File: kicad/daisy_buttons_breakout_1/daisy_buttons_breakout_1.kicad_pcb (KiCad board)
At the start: 2 copper layers, 25 parts, among them J1 Conn_01x07_Pin, SW1 SW_Push, SW10 SW_Push, SW11 SW_Push, SW12 SW_Push, SW13 SW_Push, SW14 SW_Push, SW15 SW_Push, SW16 SW_Push, SW17 SW_Push, SW18 SW_Push, SW19 SW_Push, SW2 SW_Push, SW20 SW_Push, SW3 SW_Push, SW4 SW_Push, SW5 SW_Push, SW6 SW_Push, SW7 SW_Push, SW8 SW_Push, SW9 SW_Push, U1 MCP23017x-x-SO

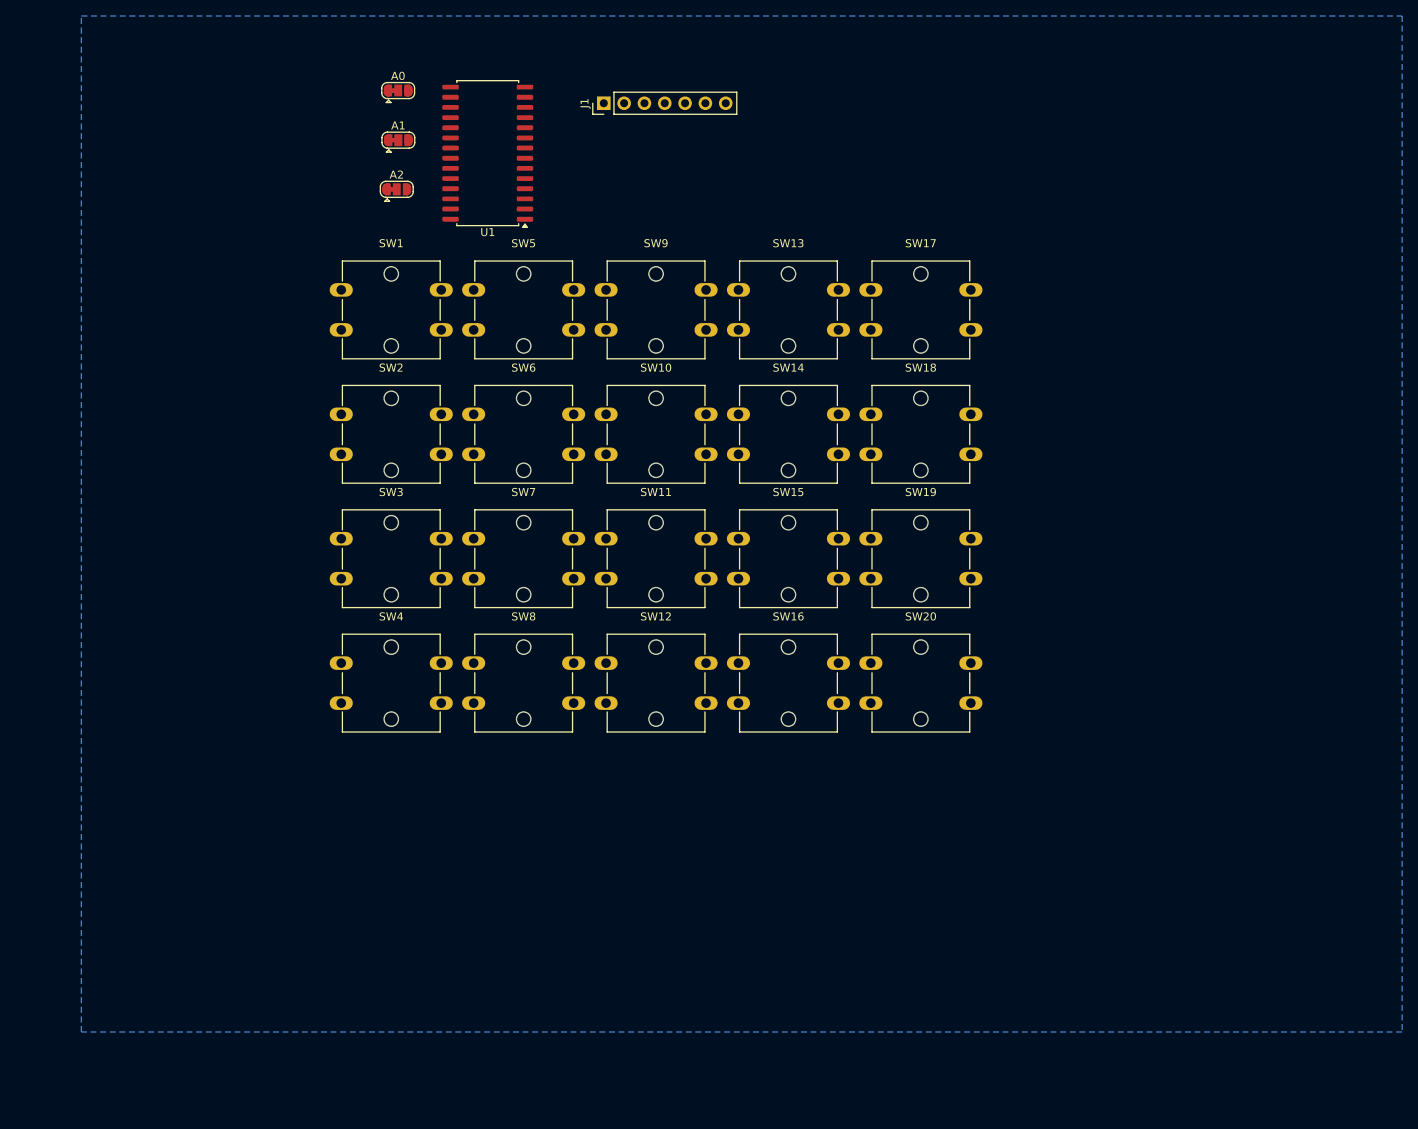
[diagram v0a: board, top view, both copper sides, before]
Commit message: Finish carrier PCB for daisy
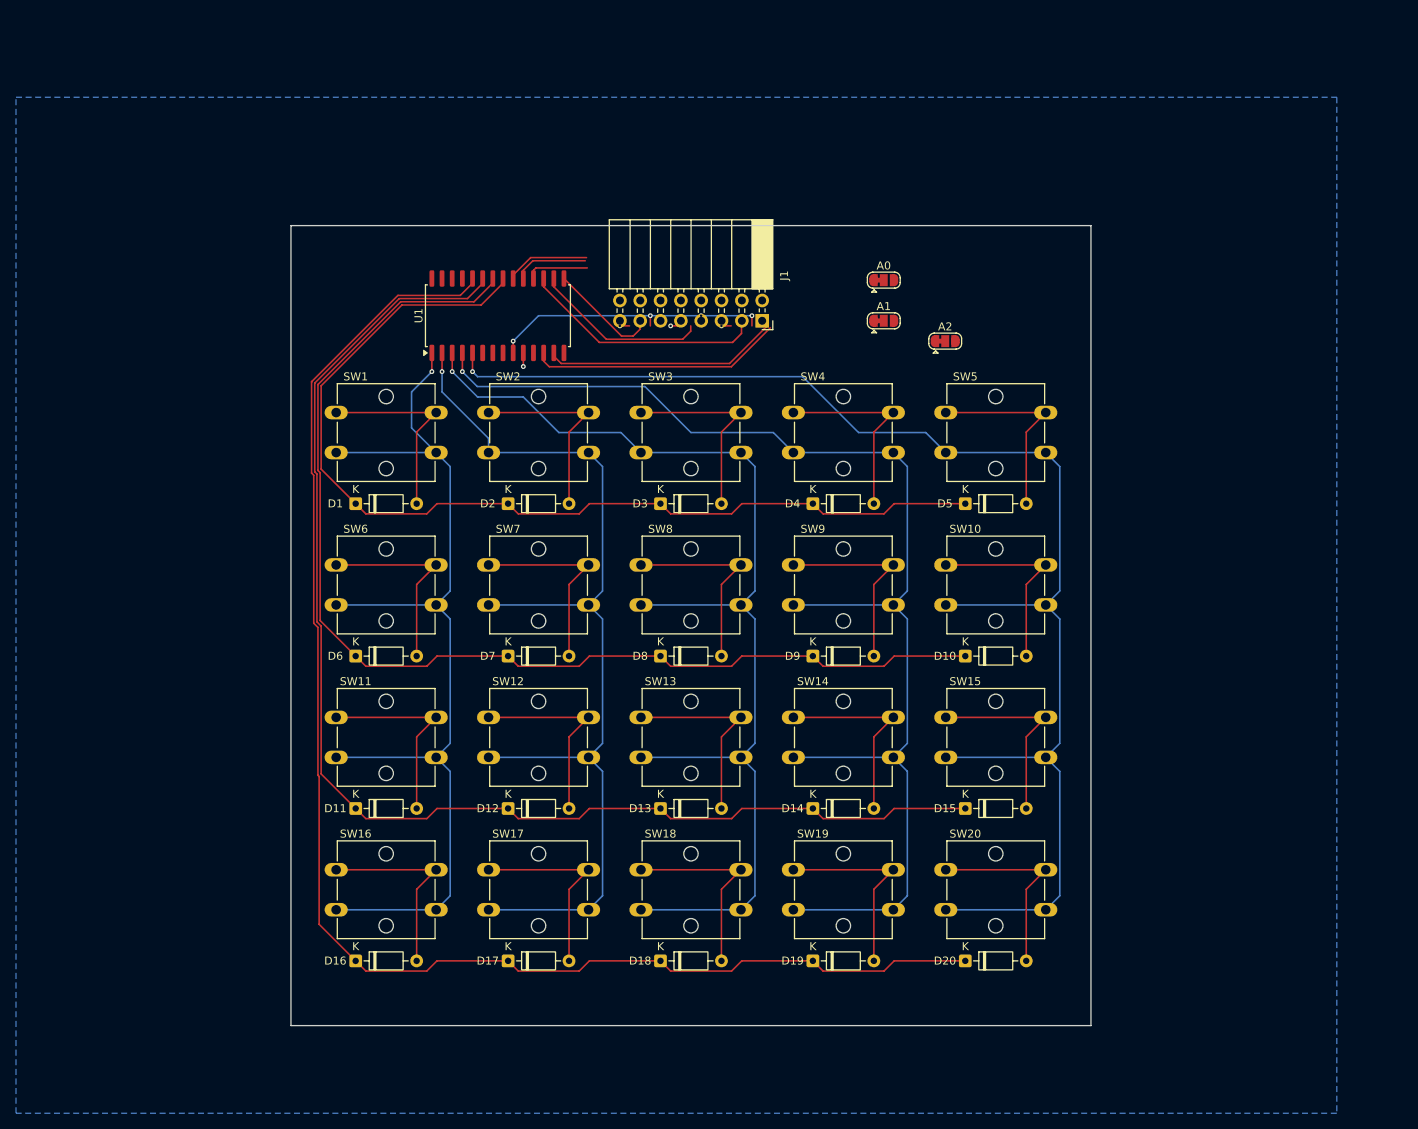
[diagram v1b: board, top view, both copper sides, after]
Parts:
- added D1: D, Diode_THT:D_DO-35_SOD27_P7.62mm_Horizontal, F.Cu at (85.1, 86.4)
- added D10: D, Diode_THT:D_DO-35_SOD27_P7.62mm_Horizontal, F.Cu at (161.3, 105.4)
- added D11: D, Diode_THT:D_DO-35_SOD27_P7.62mm_Horizontal, F.Cu at (85.1, 124.5)
- added D12: D, Diode_THT:D_DO-35_SOD27_P7.62mm_Horizontal, F.Cu at (104.1, 124.5)
- added D13: D, Diode_THT:D_DO-35_SOD27_P7.62mm_Horizontal, F.Cu at (123.2, 124.5)
- added D14: D, Diode_THT:D_DO-35_SOD27_P7.62mm_Horizontal, F.Cu at (142.2, 124.5)
- added D15: D, Diode_THT:D_DO-35_SOD27_P7.62mm_Horizontal, F.Cu at (161.3, 124.5)
- added D16: D, Diode_THT:D_DO-35_SOD27_P7.62mm_Horizontal, F.Cu at (85.1, 143.5)
- added D17: D, Diode_THT:D_DO-35_SOD27_P7.62mm_Horizontal, F.Cu at (104.1, 143.5)
- added D18: D, Diode_THT:D_DO-35_SOD27_P7.62mm_Horizontal, F.Cu at (123.2, 143.5)
- added D19: D, Diode_THT:D_DO-35_SOD27_P7.62mm_Horizontal, F.Cu at (142.2, 143.5)
- added D2: D, Diode_THT:D_DO-35_SOD27_P7.62mm_Horizontal, F.Cu at (104.1, 86.4)
- added D20: D, Diode_THT:D_DO-35_SOD27_P7.62mm_Horizontal, F.Cu at (161.3, 143.5)
- added D3: D, Diode_THT:D_DO-35_SOD27_P7.62mm_Horizontal, F.Cu at (123.2, 86.4)
- added D4: D, Diode_THT:D_DO-35_SOD27_P7.62mm_Horizontal, F.Cu at (142.2, 86.4)
- added D5: D, Diode_THT:D_DO-35_SOD27_P7.62mm_Horizontal, F.Cu at (161.3, 86.4)
- added D6: D, Diode_THT:D_DO-35_SOD27_P7.62mm_Horizontal, F.Cu at (85.1, 105.4)
- added D7: D, Diode_THT:D_DO-35_SOD27_P7.62mm_Horizontal, F.Cu at (104.1, 105.4)
- added D8: D, Diode_THT:D_DO-35_SOD27_P7.62mm_Horizontal, F.Cu at (123.2, 105.4)
- added D9: D, Diode_THT:D_DO-35_SOD27_P7.62mm_Horizontal, F.Cu at (142.2, 105.4)
- J1: value Conn_01x07_Pin -> Conn_02x08_Odd_Even; footprint Connector_PinHeader_2.54mm:PinHeader_1x07_P2.54mm_Vertical -> Connector_PinSocket_2.54mm:PinSocket_2x08_P2.54mm_Horizontal
- moved SW17 86.8 mm to (101.7, 132.1)
- moved A2 71.1 mm to (158.8, 66.0)
- moved A0 65.2 mm to (151.1, 58.4)
- moved A1 64.7 mm to (151.1, 63.5)
- moved SW4 64.6 mm to (139.8, 75.0)
- moved SW18 63.8 mm to (120.8, 132.1)
- moved SW5 61.0 mm to (158.8, 75.0)
- moved SW16 56.5 mm to (82.7, 132.1)
- moved SW13 54.8 mm to (120.8, 113.1)
- moved SW10 46.5 mm to (158.8, 94.0)
- moved SW19 42.5 mm to (139.8, 132.1)
- moved SW9 41.6 mm to (139.8, 94.0)
- moved SW3 40.6 mm to (120.8, 75.0)
- moved SW11 40.5 mm to (82.7, 113.1)
- moved SW14 38.5 mm to (139.8, 113.1)
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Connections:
- J1 pad 2: VCC -> unconnected-(J1-Pin_2-Pad2)
- J1 pad 3: /SCK -> GND
- J1 pad 4: /SDA -> unconnected-(J1-Pin_4-Pad4)
- J1 pad 5: /INT_A -> unconnected-(J1-Pin_5-Pad5)
- J1 pad 6: /INT_B -> unconnected-(J1-Pin_6-Pad6)
- J1 pad 7: /RST -> unconnected-(J1-Pin_7-Pad7)
- SW1 pad 1: unconnected-(SW1-Pad1) -> Net-(D1-A)
- SW1 pad 2: unconnected-(SW1-Pad2) -> /B0
- SW10 pad 1: unconnected-(SW10-Pad1) -> Net-(D10-A)
- SW10 pad 2: unconnected-(SW10-Pad2) -> /B4
- SW11 pad 1: unconnected-(SW11-Pad1) -> Net-(D11-A)
- SW11 pad 2: unconnected-(SW11-Pad2) -> /B0
- SW12 pad 1: unconnected-(SW12-Pad1) -> Net-(D12-A)
- SW12 pad 2: unconnected-(SW12-Pad2) -> /B1
- SW13 pad 1: unconnected-(SW13-Pad1) -> Net-(D13-A)
- SW13 pad 2: unconnected-(SW13-Pad2) -> /B2
- SW14 pad 1: unconnected-(SW14-Pad1) -> Net-(D14-A)
- SW14 pad 2: unconnected-(SW14-Pad2) -> /B3
- SW15 pad 1: unconnected-(SW15-Pad1) -> Net-(D15-A)
- SW15 pad 2: unconnected-(SW15-Pad2) -> /B4
- SW16 pad 1: unconnected-(SW16-Pad1) -> Net-(D16-A)
- SW16 pad 2: unconnected-(SW16-Pad2) -> /B0
- SW17 pad 1: unconnected-(SW17-Pad1) -> Net-(D17-A)
- SW17 pad 2: unconnected-(SW17-Pad2) -> /B1
- SW18 pad 1: unconnected-(SW18-Pad1) -> Net-(D18-A)
- SW18 pad 2: unconnected-(SW18-Pad2) -> /B2
- SW19 pad 1: unconnected-(SW19-Pad1) -> Net-(D19-A)
- SW19 pad 2: unconnected-(SW19-Pad2) -> /B3
- SW2 pad 1: unconnected-(SW2-Pad1) -> Net-(D2-A)
- SW2 pad 2: unconnected-(SW2-Pad2) -> /B1
- SW20 pad 1: unconnected-(SW20-Pad1) -> Net-(D20-A)
- SW20 pad 2: unconnected-(SW20-Pad2) -> /B4
- SW3 pad 1: unconnected-(SW3-Pad1) -> Net-(D3-A)
- SW3 pad 2: unconnected-(SW3-Pad2) -> /B2
- SW4 pad 1: unconnected-(SW4-Pad1) -> Net-(D4-A)
- SW4 pad 2: unconnected-(SW4-Pad2) -> /B3
- SW5 pad 1: unconnected-(SW5-Pad1) -> Net-(D5-A)
- SW5 pad 2: unconnected-(SW5-Pad2) -> /B4
- SW6 pad 1: unconnected-(SW6-Pad1) -> Net-(D6-A)
- SW6 pad 2: unconnected-(SW6-Pad2) -> /B0
- SW7 pad 1: unconnected-(SW7-Pad1) -> Net-(D7-A)
- SW7 pad 2: unconnected-(SW7-Pad2) -> /B1
- SW8 pad 1: unconnected-(SW8-Pad1) -> Net-(D8-A)
- SW8 pad 2: unconnected-(SW8-Pad2) -> /B2
- SW9 pad 1: unconnected-(SW9-Pad1) -> Net-(D9-A)
- SW9 pad 2: unconnected-(SW9-Pad2) -> /B3
- U1 pad 1: unconnected-(U1-GPB0-Pad1) -> /B0
- U1 pad 2: unconnected-(U1-GPB1-Pad2) -> /B1
- U1 pad 21: unconnected-(U1-GPA0-Pad21) -> /A0
- U1 pad 22: unconnected-(U1-GPA1-Pad22) -> /A1
- U1 pad 23: unconnected-(U1-GPA2-Pad23) -> /A2
- U1 pad 24: unconnected-(U1-GPA3-Pad24) -> /A3
- U1 pad 25: unconnected-(U1-GPA4-Pad25) -> /A4
- U1 pad 26: unconnected-(U1-GPA5-Pad26) -> /A5
- U1 pad 27: unconnected-(U1-GPA6-Pad27) -> /A6
- U1 pad 28: unconnected-(U1-GPA7-Pad28) -> /A7
- U1 pad 3: unconnected-(U1-GPB2-Pad3) -> /B2
- U1 pad 4: unconnected-(U1-GPB3-Pad4) -> /B3
- U1 pad 5: unconnected-(U1-GPB4-Pad5) -> /B4
- U1 pad 6: unconnected-(U1-GPB5-Pad6) -> /B5
- U1 pad 7: unconnected-(U1-GPB6-Pad7) -> /B6
- U1 pad 8: unconnected-(U1-GPB7-Pad8) -> /B7
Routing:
- net /A3: track 0.00 -> 180.9 mm
- net /B4: track 0.00 -> 177.2 mm, vias 0 -> 1
- net /A2: track 0.00 -> 162.5 mm
- net /B3: track 0.00 -> 159.4 mm, vias 0 -> 1
- net /A1: track 0.00 -> 144.0 mm
- net /B2: track 0.00 -> 141.6 mm, vias 0 -> 1
- net /B1: track 0.00 -> 126.4 mm, vias 0 -> 1
- net /B0: track 0.00 -> 126.3 mm, vias 0 -> 1
- net /A0: track 0.00 -> 125.6 mm
- net VCC: track 0.00 -> 36.4 mm, vias 0 -> 4
- net /SCK: track 0.00 -> 31.7 mm
- net Net-(A2-C): track 0.00 -> 30.1 mm
- net /SDA: track 0.00 -> 29.4 mm
- net Net-(D6-A): track 0.00 -> 24.9 mm
- net Net-(D1-A): track 0.00 -> 24.9 mm
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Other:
- board outline added: 100 x 100 mm

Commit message: Make side boards for pots and buttons use same connector as main board
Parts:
- added C1: 100nF, C_0603_1608Metric_Pad1.08x0.95mm_HandSolder, F.Cu at (98.4, 72.0)
- added R1: 10k, R_0603_1608Metric_Pad0.98x0.95mm_HandSolder, F.Cu at (107.3, 54.9)
- added REF**: MountingHole_3.2mm_M3_Pad, MountingHole_3.2mm_M3_Pad, F.Cu at (81.3, 55.9)
- added REF**: MountingHole_3.2mm_M3_Pad, MountingHole_3.2mm_M3_Pad, F.Cu at (172.7, 55.9)
- added REF**: MountingHole_3.2mm_M3_Pad, MountingHole_3.2mm_M3_Pad, F.Cu at (81.3, 147.3)
- added REF**: MountingHole_3.2mm_M3_Pad, MountingHole_3.2mm_M3_Pad, F.Cu at (172.7, 147.3)
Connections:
- J1 pad 10: unconnected-(J1-Pin_10-Pad10) -> /INT_A
- J1 pad 11: unconnected-(J1-Pin_11-Pad11) -> /RST
- J1 pad 13: unconnected-(J1-Pin_13-Pad13) -> GND
- J1 pad 16: unconnected-(J1-Pin_16-Pad16) -> GND
- J1 pad 4: unconnected-(J1-Pin_4-Pad4) -> VCC
- J1 pad 5: unconnected-(J1-Pin_5-Pad5) -> /SDA
- J1 pad 6: unconnected-(J1-Pin_6-Pad6) -> /SCK
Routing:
- net VCC: track 36.4 -> 111.6 mm
- net Net-(A1-C): track 21.9 -> 60.8 mm
- net Net-(A2-C): track 30.1 -> 64.1 mm
- net Net-(A0-C): track 13.3 -> 43.8 mm
- net /RST: track 7.87 -> 28.2 mm, vias 0 -> 2
- net /SCK: track 31.7 -> 50.3 mm
- net /INT_A: track 10.5 -> 28.9 mm, vias 0 -> 1
- net GND: track 5.33 -> 17.1 mm
- net /INT_B: track 9.26 -> 0.00 mm
- net /SDA: track 29.4 -> 26.7 mm

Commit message: Finish breakout periph boards and add gerbers
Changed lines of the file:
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@@
 			(outputformat 1)
 			(mirror no)
-			(drillshape 1)
+			(drillshape 0)
 			(scaleselection 1)
-			(outputdirectory "")
+			(outputdirectory "daisy_buttons_breakout_1_v0_gerbers/")
 		)
 	)
@@
 		(sheetname "/")
 		(sheetfile "daisy_buttons_breakout_1.kicad_sch")
-		(units
-			(unit
-				(name "A")
-				(pins "1" "3" "5" "7" "9" "11" "13" "15" "2" "4" "6" "8" "10" "12" "14"
-					"16"
-				)
-			)
-		)
 		(attr through_hole)
 		(duplicate_pad_numbers_are_jumpers no)
 		(fp_line
-			(start -12.63 19.11)
+			(start -10 19.11)
 			(end -4.000001 19.11)
 			(stroke
@@
 		)
 		(fp_line
-			(start -12.630001 16.51)
+			(start -10 16.51)
 			(end -4 16.51)
 			(stroke
@@
 		)
 		(fp_line
-			(start -12.63 13.97)
+			(start -10 13.97)
 			(end -4 13.97)
 			(stroke
@@
 		)
 		(fp_line
-			(start -12.63 11.43)
+			(start -10 11.43)
 			(end -4.000001 11.43)
 			(stroke
@@
 		)
 		(fp_line
-			(start -12.63 8.89)
+			(start -10 8.89)
 			(end -4 8.89)
 			(stroke
@@
 		)
 		(fp_line
-			(start -12.630001 6.35)
+			(start -10 6.35)
 			(end -4 6.35)
 			(stroke
@@
 		)
 		(fp_line
-			(start -12.63 3.81)
+			(start -10 3.81)
 			(end -4 3.81)
 			(stroke
@@
 		)
 		(fp_line
-			(start -12.63 1.27)
+			(start -10 1.27)
 			(end -4.000001 1.27)
 			(stroke
@@
 		)
 		(fp_line
-			(start -12.63 1.151905)
+			(start -10 1.151905)
 			(end -4 1.151905)
 			(stroke
@@
 		)
 		(fp_line
-			(start -12.630001 1.03381)
+			(start -10 1.03381)
 			(end -4 1.03381)
 			(stroke
@@
 		)
 		(fp_line
-			(start -12.63 0.915714)
+			(start -10 0.915714)
 			(end -4.000001 0.915714)
 			(stroke
@@
 		)
 		(fp_line
-			(start -12.63 0.797619)
+			(start -10 0.797619)
 			(end -4 0.797619)
 			(stroke
@@
 		)
 		(fp_line
-			(start -12.630001 0.679524)
+			(start -10 0.679524)
 			(end -4 0.679524)
 			(stroke
@@
 		)
 		(fp_line
-			(start -12.63 0.561429)
+			(start -10 0.561429)
 			(end -4 0.561429)
 			(stroke
@@
 		)
 		(fp_line
-			(start -12.63 0.443333)
+			(start -10 0.443333)
 			(end -4 0.443333)
 			(stroke
@@
 		)
 		(fp_line
-			(start -12.630001 0.325238)
+			(start -10 0.325238)
 			(end -4 0.325238)
 			(stroke
@@
 		)
 		(fp_line
-			(start -12.63 0.207143)
+			(start -10 0.207143)
 			(end -4 0.207143)
 			(stroke
@@
 		)
 		(fp_line
-			(start -12.63 0.089048)
+			(start -10 0.089048)
 			(end -4.000001 0.089048)
 			(stroke
@@
 		)
 		(fp_line
-			(start -12.630001 -0.029048)
+			(start -10 -0.029048)
 			(end -4 -0.029048)
 			(stroke
@@
 		)
 		(fp_line
-			(start -12.63 -0.147143)
+			(start -10 -0.147143)
 			(end -4 -0.147143)
 			(stroke
@@
 		)
 		(fp_line
-			(start -12.63 -0.265238)
+			(start -10 -0.265238)
 			(end -4.000001 -0.265238)
 			(stroke
@@
 		)
 		(fp_line
-			(start -12.63 -0.383333)
+			(start -10 -0.383332)
 			(end -4 -0.383332)
 			(stroke
@@
 		)
 		(fp_line
-			(start -12.63 -0.501429)
+			(start -10 -0.501429)
 			(end -4 -0.501429)
 			(stroke
@@
 		)
 		(fp_line
-			(start -12.63 -0.619524)
+			(start -10 -0.619524)
 			(end -4.000001 -0.619524)
 			(stroke
@@
 		)
 		(fp_line
-			(start -12.63 -0.737619)
+			(start -10 -0.737619)
 			(end -4.000001 -0.737619)
 			(stroke
@@
 		)
 		(fp_line
-			(start -12.63 -0.855714)
+			(start -10 -0.855714)
 			(end -4 -0.855714)
 			(stroke
@@
 		)
 		(fp_line
-			(start -12.63 -0.97381)
+			(start -10 -0.97381)
 			(end -4 -0.97381)
 			(stroke
@@
 		)
 		(fp_line
-			(start -12.63 -1.091905)
+			(start -10 -1.091905)
 			(end -4.000001 -1.091905)
 			(stroke
@@
 		)
 		(fp_line
-			(start -12.63 -1.21)
+			(start -10 -1.21)
 			(end -4 -1.21)
 			(stroke
@@
 		)
 		(fp_line
-			(start -12.630001 -1.33)
-			(end -12.63 19.11)
+			(start -10 -1.33)
+			(end -9.999999 19.11)
 			(stroke
 				(width 0.12)
@@
 		)
 		(fp_line
-			(start -12.630001 -1.33)
+			(start -10 -1.33)
 			(end -4 -1.33)
 			(stroke
@@
 		)
 		(fp_line
-			(start -12.57 19.05)
-			(end -12.57 -1.27)
+			(start -10 19.05)
+			(end -10 -1.27)
 			(stroke
 				(width 0.1)
@@
 		(fp_line
 			(start -4.06 19.05)
-			(end -12.57 19.05)
+			(end -10 19.05)
 			(stroke
 				(width 0.1)
@@
 		)
 		(fp_line
-			(start -12.57 -1.27)
+			(start -10 -1.270001)
 			(end -5.03 -1.270001)
 			(stroke
@@
 		(tags "mountinghole M3")
 		(property "Reference" "REF**"
-			(at 0 -4.15 0)
+			(at 0 4.572 0)
 			(layer "F.SilkS")
 			(effects
@@
 		(tags "mountinghole M3")
 		(property "Reference" "REF**"
-			(at 0 -4.15 0)
+			(at 0.254 4.572 0)
 			(layer "F.SilkS")
 			(effects
@@
 		(tags "mountinghole M3")
 		(property "Reference" "REF**"
-			(at 0 -4.15 0)
+			(at 5.842 0 0)
 			(layer "F.SilkS")
 			(effects
@@
 		(tags "mountinghole M3")
 		(property "Reference" "REF**"
-			(at 0 -4.15 0)
+			(at -5.588 0.508 0)
 			(layer "F.SilkS")
 			(effects
